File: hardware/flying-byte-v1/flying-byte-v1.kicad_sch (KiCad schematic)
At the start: 0 parts

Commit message: feature: Add the MCU power and decoupling
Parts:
- added C1, C8: 4u7, symbol Device:C_Small
- added C10, C2, C3, C4, C5, C6, C7, C9: 100n, symbol Device:C_Small
- added U1: STM32WB55CEU6, Package_DFN_QFN:QFN-48-1EP_7x7mm_P0.5mm_EP5.6x5.6mm, symbol MCU_ST_STM32WB:STM32WB55CEUx
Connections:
- new net +3V3: C1.1, C10.1, C2.1, C3.1, C4.1, C5.1, C6.1, C7.1, C8.1, C9.1, U1.1 (VBAT), U1.20 (VDD), U1.23 (VDDRF), U1.34 (VDDSMPS), U1.35 (VDD), U1.40 (VDDUSB), U1.48 (VDD), U1.8 (VDDA)
- new net GND: C1.2, C10.2, C2.2, C3.2, C4.2, C5.2, C6.2, C7.2, C8.2, C9.2, U1.22 (VSSRF), U1.32 (VSSSMPS), U1.49 (VSS)

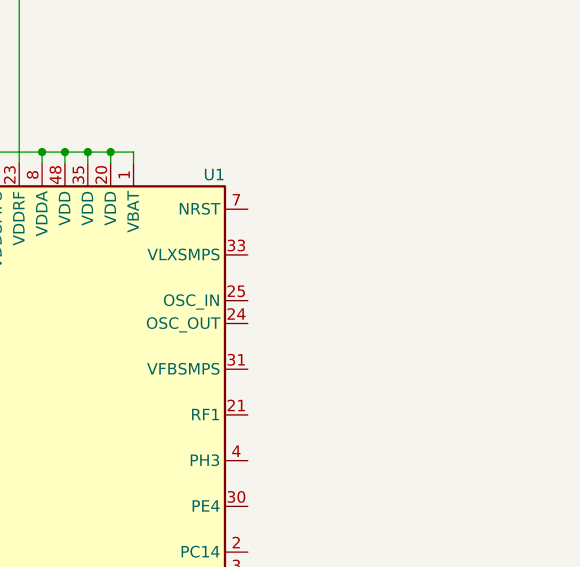
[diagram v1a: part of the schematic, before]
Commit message: feature: Add the MCU SMPS
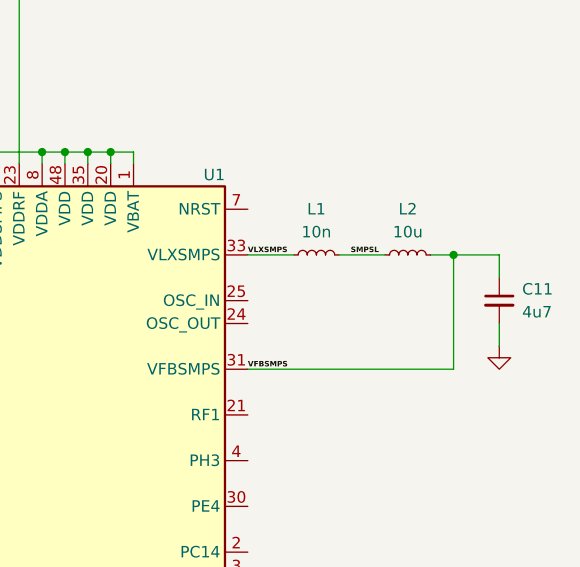
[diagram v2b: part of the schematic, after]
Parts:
- added C11: 4u7, symbol Device:C_Small
- added L1: 10n, symbol Device:L_Small
- added L2: 10u, symbol Device:L_Small
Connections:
- net GND: now also C11.2
- net VFBSMPS: now reaches U1.31 (VFBSMPS)
- net VFBSMPS: now also C11.1, L2.2
- net VLXSMPS: now reaches U1.33 (VLXSMPS)
- net VLXSMPS: now also L1.1
- new net SMPSL: L1.2, L2.1
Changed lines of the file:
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@@
   (junction (at 90.17 43.18) (diameter 0) (color 0 0 0 0)
   )
+  (junction (at 204.47 68.58) (diameter 0) (color 0 0 0 0)
+  )
   (junction (at 110.49 50.8) (diameter 0) (color 0 0 0 0)
   )
@@
     (stroke (width 0) (type default))
   )
+  (wire (pts (xy 204.47 68.58) (xy 204.47 81.28))
+    (stroke (width 0) (type default))
+  )
   (wire (pts (xy 161.29 58.42) (xy 161.29 57.15))
     (stroke (width 0) (type default))
@@
     (stroke (width 0) (type default))
   )
+  (wire (pts (xy 181.61 81.28) (xy 204.47 81.28))
+    (stroke (width 0) (type default))
+  )
   (wire (pts (xy 156.21 138.43) (xy 156.21 139.7))
     (stroke (width 0) (type default))
@@
     (stroke (width 0) (type default))
   )
+  (wire (pts (xy 191.77 68.58) (xy 196.85 68.58))
+    (stroke (width 0) (type default))
+  )
   (wire (pts (xy 120.65 43.18) (xy 110.49 43.18))
     (stroke (width 0) (type default))
@@
     (stroke (width 0) (type default))
   )
+  (wire (pts (xy 181.61 68.58) (xy 186.69 68.58))
+    (stroke (width 0) (type default))
+  )
   (wire (pts (xy 151.13 57.15) (xy 158.75 57.15))
     (stroke (width 0) (type default))
@@
     (stroke (width 0) (type default))
   )
+  (wire (pts (xy 209.55 71.12) (xy 209.55 68.58))
+    (stroke (width 0) (type default))
+  )
   (wire (pts (xy 163.83 57.15) (xy 166.37 57.15))
     (stroke (width 0) (type default))
@@
     (stroke (width 0) (type default))
   )
+  (wire (pts (xy 201.93 68.58) (xy 204.47 68.58))
+    (stroke (width 0) (type default))
+  )
   (wire (pts (xy 130.81 36.83) (xy 130.81 38.1))
     (stroke (width 0) (type default))
@@
     (stroke (width 0) (type default))
   )
+  (wire (pts (xy 209.55 76.2) (xy 209.55 78.74))
+    (stroke (width 0) (type default))
+  )
   (wire (pts (xy 130.81 43.18) (xy 120.65 43.18))
     (stroke (width 0) (type default))
@@
     (stroke (width 0) (type default))
   )
+  (wire (pts (xy 204.47 68.58) (xy 209.55 68.58))
+    (stroke (width 0) (type default))
+  )
   (wire (pts (xy 130.81 30.48) (xy 130.81 29.21))
     (stroke (width 0) (type default))
   )
+  (label "SMPSL" (at 193.04 68.58 0) (fields_autoplaced)
+    (effects (font (size 0.6 0.6) (thickness 0.21) bold) (justify left bottom))
+  )
+  (label "VLXSMPS" (at 181.61 68.58 0) (fields_autoplaced)
+    (effects (font (size 0.6 0.6) (thickness 0.21) bold) (justify left bottom))
+  )
+  (label "VFBSMPS" (at 181.61 81.28 0) (fields_autoplaced)
+    (effects (font (size 0.6 0.6) (thickness 0.21) bold) (justify left bottom))
+  )
+  (symbol (lib_id "Device:L_Small") (at 199.39 68.58 90) (unit 1)
+    (in_bom yes) (on_board yes) (dnp no) (fields_autoplaced)
+    (property "Reference" "L2" (at 199.39 63.5 90)
+      (effects (font (size 1.27 1.27)))
+    )
+    (property "Value" "10u" (at 199.39 66.04 90)
+      (effects (font (size 1.27 1.27)))
+    )
+    (property "Footprint" "" (at 199.39 68.58 0)
+      (effects (font (size 1.27 1.27)) hide)
+    )
+    (property "Datasheet" "~" (at 199.39 68.58 0)
+      (effects (font (size 1.27 1.27)) hide)
+    )
+    (pin "1")
+    (pin "2")
+    (instances
+      (project "flying-byte-v1"
+        (path "/89251f6d-2a03-4ee6-93f4-15acd18dfc68"
+          (reference "L2") (unit 1)
+        )
+      )
+    )
+  )
   (symbol (lib_id "Device:C_Small") (at 100.33 46.99 0) (unit 1)
     (in_bom yes) (on_board yes) (dnp no) (fields_autoplaced)
@@
         (path "/89251f6d-2a03-4ee6-93f4-15acd18dfc68"
           (reference "C8") (unit 1)
+        )
+      )
+    )
+  )
+  (symbol (lib_id "Device:C_Small") (at 209.55 73.66 0) (unit 1)
+    (in_bom yes) (on_board yes) (dnp no) (fields_autoplaced)
+    (property "Reference" "C11" (at 212.09 72.3963 0)
+      (effects (font (size 1.27 1.27)) (justify left))
+    )
+    (property "Value" "4u7" (at 212.09 74.9363 0)
+      (effects (font (size 1.27 1.27)) (justify left))
+    )
+    (property "Footprint" "" (at 209.55 73.66 0)
+      (effects (font (size 1.27 1.27)) hide)
+    )
+    (property "Datasheet" "~" (at 209.55 73.66 0)
+      (effects (font (size 1.27 1.27)) hide)
+    )
+    (pin "1")
+    (pin "2")
+    (instances
+      (project "flying-byte-v1"
+        (path "/89251f6d-2a03-4ee6-93f4-15acd18dfc68"
+          (reference "C11") (unit 1)
         )
       )
@@
     )
   )
+  (symbol (lib_id "Device:L_Small") (at 189.23 68.58 90) (unit 1)
+    (in_bom yes) (on_board yes) (dnp no) (fields_autoplaced)
+    (property "Reference" "L1" (at 189.23 63.5 90)
+      (effects (font (size 1.27 1.27)))
+    )
+    (property "Value" "10n" (at 189.23 66.04 90)
+      (effects (font (size 1.27 1.27)))
+    )
+    (property "Footprint" "" (at 189.23 68.58 0)
+      (effects (font (size 1.27 1.27)) hide)
+    )
+    (property "Datasheet" "~" (at 189.23 68.58 0)
+      (effects (font (size 1.27 1.27)) hide)
+    )
+    (pin "1")
+    (pin "2")
+    (instances
+      (project "flying-byte-v1"
+        (path "/89251f6d-2a03-4ee6-93f4-15acd18dfc68"
+          (reference "L1") (unit 1)
+        )
+      )
+    )
+  )
   (symbol (lib_id "power:GND") (at 130.81 38.1 0) (unit 1)
     (in_bom yes) (on_board yes) (dnp no) (fields_autoplaced)
@@
         )
       )
+    )
+  )
+  (symbol (lib_id "power:GND") (at 209.55 78.74 0) (unit 1)
+    (in_bom yes) (on_board yes) (dnp no) (fields_autoplaced)
+    (property "Reference" "#PWR08" (at 209.55 85.09 0)
+      (effects (font (size 1.27 1.27)) hide)
+    )
+    (property "Value" "GND" (at 209.55 83.82 0)
+      (effects (font (size 1.27 1.27)) hide)
+    )
+    (property "Footprint" "" (at 209.55 78.74 0)
+      (effects (font (size 1.27 1.27)) hide)
+    )
+    (property "Datasheet" "" (at 209.55 78.74 0)
+      (effects (font (size 1.27 1.27)) hide)
+    )
+    (pin "1")
+    (instances
+      (project "flying-byte-v1"
+        (path "/89251f6d-2a03-4ee6-93f4-15acd18dfc68"
+          (reference "#PWR08") (unit 1)
+        )
+      )

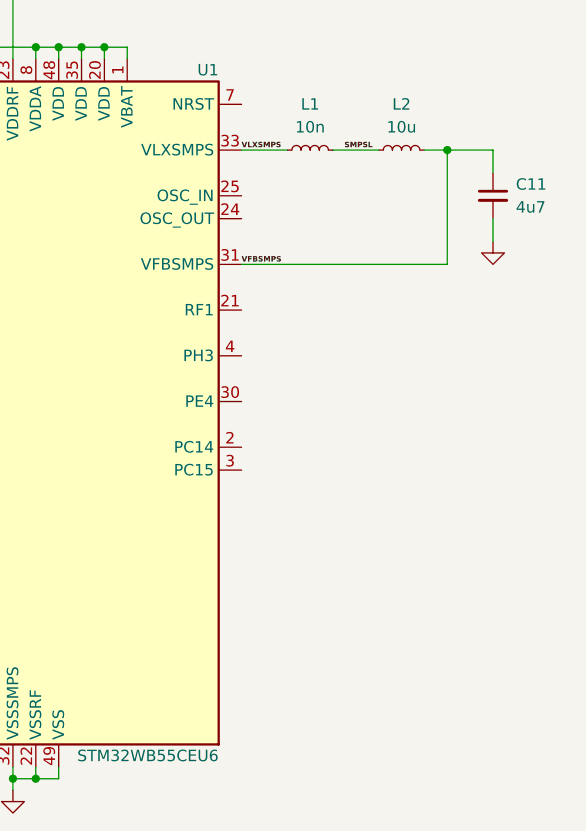
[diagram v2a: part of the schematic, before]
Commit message: feature: Add the HSE and LSE crystals
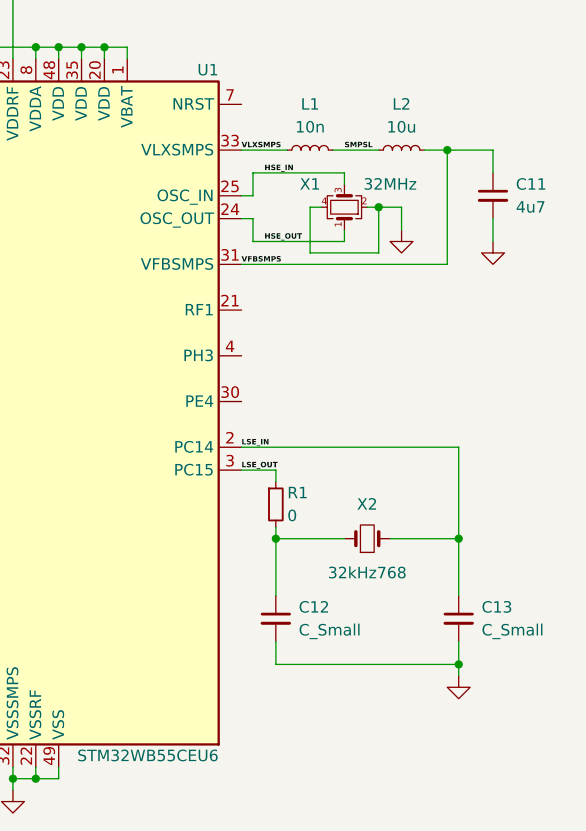
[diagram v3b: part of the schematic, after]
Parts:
- added C12, C13: C_Small, symbol Device:C_Small
- added R1: 0, symbol Device:R_Small
- added X1: 32MHz, symbol Device:Crystal_GND24_Small
- added X2: 32kHz768, symbol Device:Crystal_Small
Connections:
- net GND: now also C12.2, C13.2, X1.2, X1.4
- net LSE_IN: now reaches U1.2 (PC14)
- net LSE_IN: now also C13.1, X2.2
- net HSE_OUT: now reaches U1.24 (OSC_OUT)
- net HSE_OUT: now also X1.1
- net HSE_IN: now reaches U1.25 (OSC_IN)
- net HSE_IN: now also X1.3
- net LSE_OUT: now reaches U1.3 (PC15)
- net LSE_OUT: now also R1.1
- new net: C12.1, R1.2, X2.1

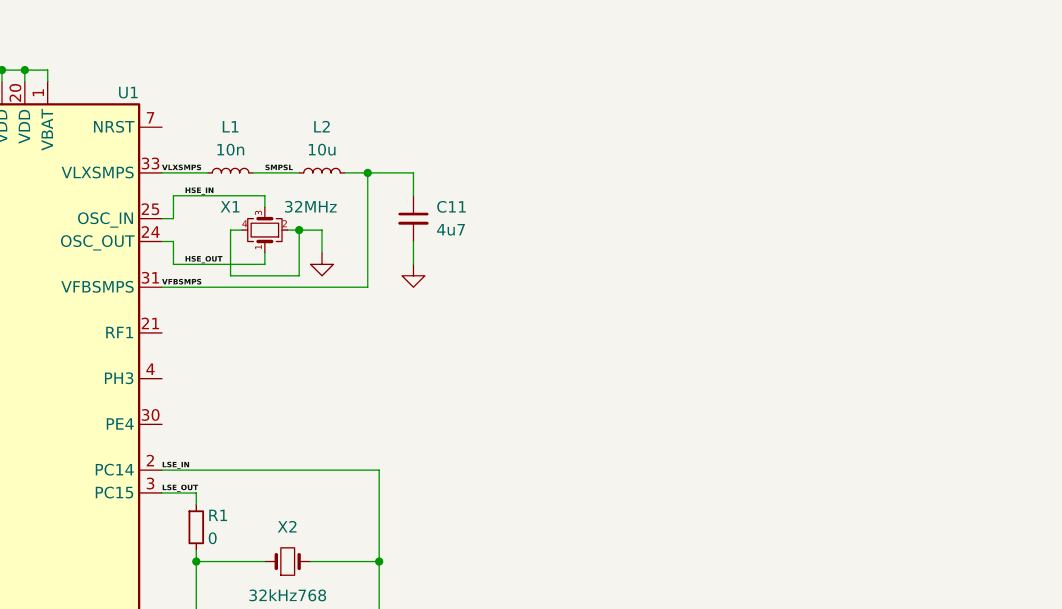
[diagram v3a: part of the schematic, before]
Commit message: feature: Add the RF section with LPF symbol and footprint
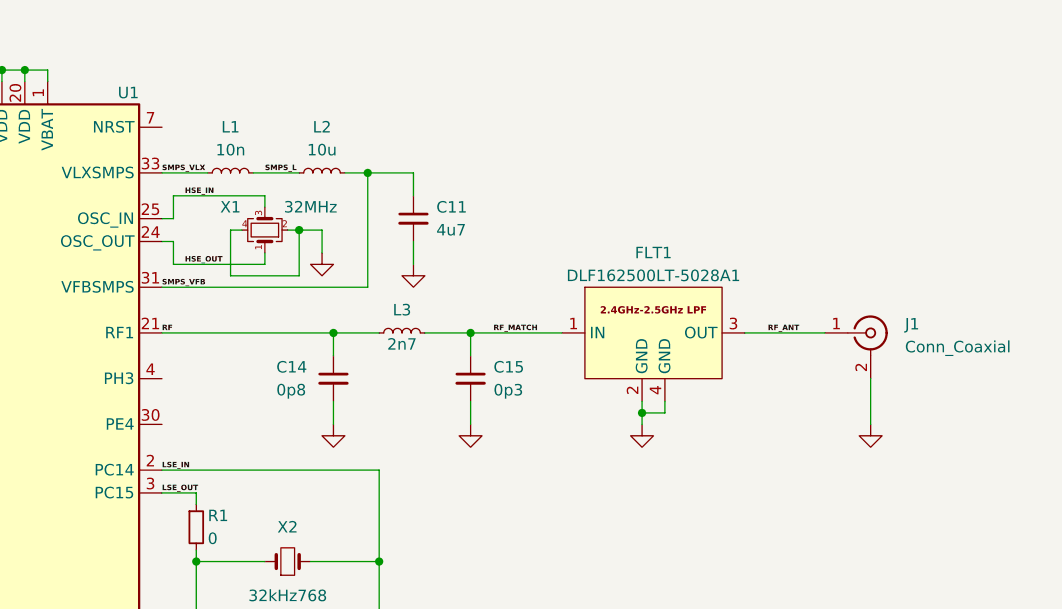
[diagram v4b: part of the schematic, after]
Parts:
- added C14: 0p8, symbol Device:C_Small
- added C15: 0p3, symbol Device:C_Small
- added FLT1: DLF162500LT-5028A1, flying-byte-v1-pcb-footprints:DLF162500LT-5028A1, symbol flying-byte-v1-schematic-symbols:DLF162500LT-5028A1
- added J1: Conn_Coaxial, symbol Connector:Conn_Coaxial
- added L3: 2n7, symbol Device:L_Small
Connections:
- net GND: now also C14.2, C15.2, FLT1.2 (GND), FLT1.4 (GND), J1.2 (Ext)
- net RF: now reaches U1.21 (RF1)
- net RF: now also C14.1, L3.1
- net SMPSL renamed SMPS_L
- net VFBSMPS renamed SMPS_VFB
- net VLXSMPS renamed SMPS_VLX
- new net RF_ANT: FLT1.3 (OUT), J1.1 (In)
- new net RF_MATCH: C15.1, FLT1.1 (IN), L3.2
